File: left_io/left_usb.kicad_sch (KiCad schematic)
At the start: 160 parts, among them J22 USB-C source-only data port J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, J23 USB-C source-only data port J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, J24 USB 3.0 Type-A internal heade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, J25 USB 2.0 Type-A internal heade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, U1700 USB7206C-I/KDX six-port USB 3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, U1701 TPS62823DLC 3A USB7206C 1.146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, U1702 TLV803EA29 USB hub reset supe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, U1703 TPS56637RPAR VSYS to USB_PORT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, U1704 SN74LVC1G08 hub 3V3/core-PG r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, U1740 TPS2553DDBVR 1.3A USB branch, U1741 TPS25810RVCR Type-C DFP contr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, U1742 HD3SS6126RUAR USB3 orientatio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, U1743 TPD1S514-1YZR 5.9V VBUS OVP, U1745 TPD4E05U06 USB2/CC ESD, U1780 TPS2553DDBVR 1.3A USB branch, U1781 TPS25810RVCR Type-C DFP contr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, U1782 HD3SS6126RUAR USB3 orientatio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, U1783 TPD1S514-1YZR 5.9V VBUS OVP, U1785 TPD4E05U06 USB2/CC ESD, U1800 TPS2553DDBVR USB3-A VBUS bran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, U1801 USBLC6-2P6 USB3-A D+/D- ESD, U1802 TPD4E05U06 USB3-A SuperSpeed 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, U1803 TPS2553DDBVR USB2-A VBUS bran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, U1804 USBLC6-2P6 USB2-A D+/D- ESD, Y1700 25.000MHz 3.3V USB hub oscill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

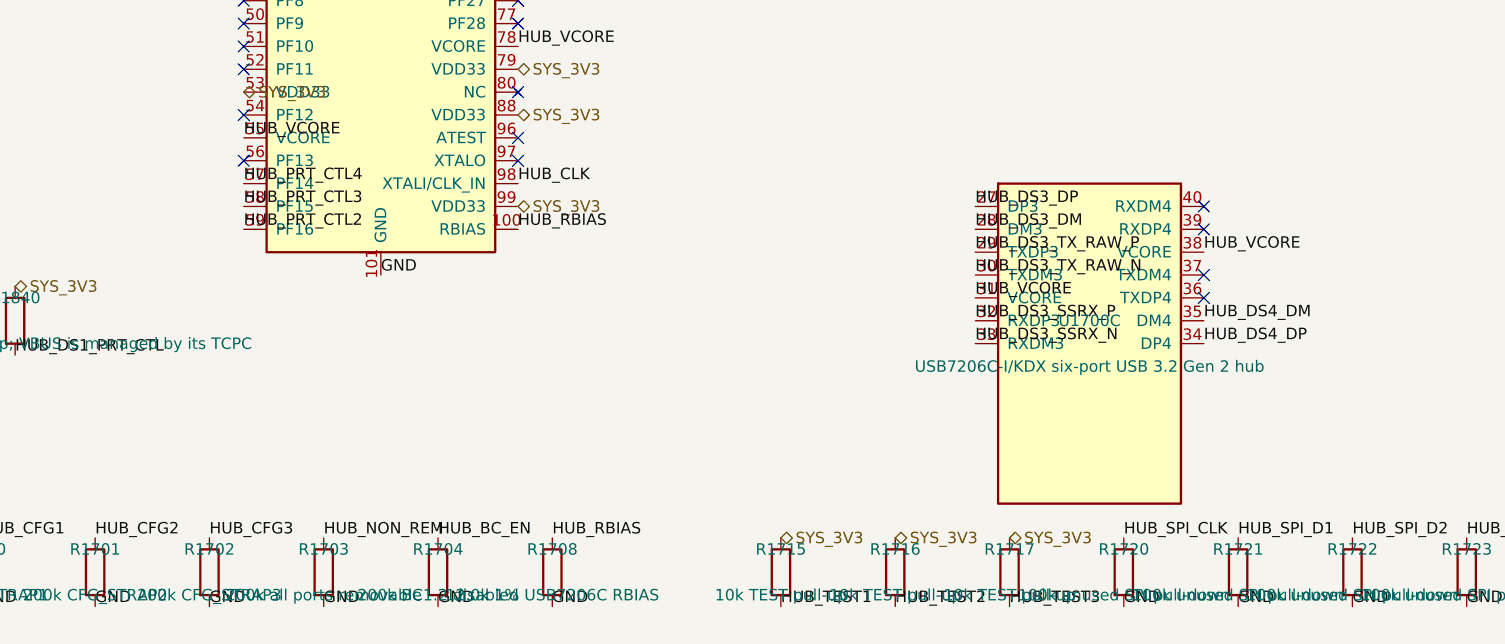
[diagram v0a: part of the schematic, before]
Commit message: Phase 5: second-opinion audit remediation + rebuilt, verified board pipeline
Second-opinion AI audit found A-tier defects; remediation applied and the
board pipeline rebuilt on a known-good base with the fixes it needed:

- electrical: LTC4418IUF symbol pinout corrected (both selectors were
  dead as drawn); center charge cascade (U15 <- U15B, PD1 > PD2 > AUX);
  pack negative never crosses FPC-3, 15-pin FG_VSS return; power-budgeted
  FPC pin maps (0.4 A/pin derate); J12/DS4 completed; AUX source fuse
- FH41-68S footprint: 13 datasheet-correct SH pads + SH pin in symbol
- connector geometry settled against the Hirose FH12 2D drawing: FFC
  enters opposite the solder pins (mouth = local +Y); reversed side-B
  maps are correct for the 180-deg-mounted pairs; rotations set so mouths
  face across every seam
- pipeline (generate_split_boards.py): per-pin pad-net resync from the
  netlists (kills shadow nets for good), netlist-exact name
  normalization, netlist-only part injection (cascade, probe headers),
  zone refill after outline swap, read-before-write race fixed, orphan
  parts dropped loudly, non-zero exit on unresolved overlaps
- monolith board relocated to old/monolith_ducktop2.kicad_pcb (placement
  oracle for the center cut only)

verified end state: 4 boards 0 shorts / 0 clearance / 0 drill, 0 boundary
crossings, 6/6 connectors contract-exact with mouths facing, 0 shadow
nets, gates PASS x4, ERC 0 x4. routing next (499 nets/board).
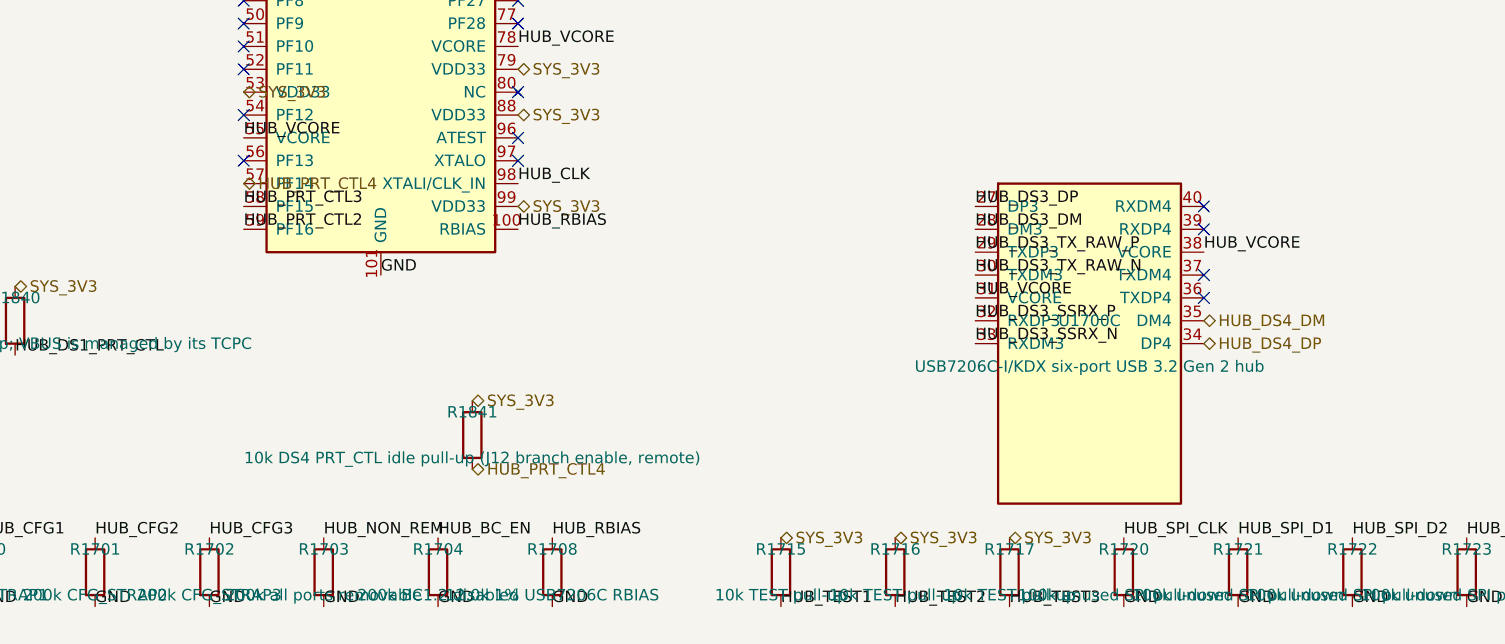
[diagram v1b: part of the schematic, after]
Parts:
- removed C1716: 100n oscillator bypass, Capacitor_SMD:C_0603_1608Metric, symbol Device:C
- removed C1717: 100n hub reset-gate bypass, Capacitor_SMD:C_0603_1608Metric, symbol Device:C
- removed C1740, C1780: 100n branch input, Capacitor_SMD:C_0603_1608Metric, symbol Device:C
- removed C1852: 100n C0G USB3-A SSTX+ series AC, Capacitor_SMD:C_0402_1005Metric, symbol Device:C
- removed R1700: 10k CFG_STRAP1, Resistor_SMD:R_0603_1608Metric, symbol Device:R
- removed R1718: 10k hub 3V3 supervisor pull-up, Resistor_SMD:R_0603_1608Metric, symbol Device:R
- removed R1740, R1780, R1850, R1851: 20.0k 1% TPS2553 1.3A ILIM, Resistor_SMD:R_0603_1608Metric, symbol Device:R
- added C1849: 10u USB7206C VDD33 bulk, Capacitor_SMD:C_0805_2012Metric, symbol Device:C
- added J24: USB 3.0 Type-A internal header (hub DIS5), Connector_USB:USB_A_Receptacle_XKB_U231-091N-4BLRA00-S, symbol USB3_A:USB3_A
- added R1723: 100k unused SPI pull-down, Resistor_SMD:R_0603_1608Metric, symbol Device:R
- added unit 2 of U1700
- added U1704: SN74LVC1G08 hub 3V3/core-PG reset gate, Package_TO_SOT_SMD:SOT-23-5, symbol 74xGxx:74LVC1G08
- added U1741, U1781: TPS25810RVCR Type-C DFP controller, Package_DFN_QFN:Texas_RVC0020A_WQFN-20-1EP_3x4mm_P0.5mm_EP1.6x2.6mm, symbol Interface_USB:TPS25810RVC
- added U1745, U1785: TPD4E05U06 USB2/CC ESD, Package_SON:USON-10_2.5x1.0mm_P0.5mm, symbol Power_Protection:TPD4E05U06DQA
- added U1801: USBLC6-2P6 USB3-A D+/D- ESD, Package_TO_SOT_SMD:SOT-666, symbol Power_Protection:USBLC6-2P6
- added U1804: USBLC6-2P6 USB2-A D+/D- ESD, Package_TO_SOT_SMD:SOT-666, symbol Power_Protection:USBLC6-2P6
- added Y1700: 25.000MHz 3.3V USB hub oscillator, Oscillator:Oscillator_SMD_Abracon_ASDMB-4Pin_2.5x2.0mm, symbol Oscillator:ASDMB-xxxMHz
- C1716: renamed from C1722; value 100n USB 3.2 TX AC coupling -> 100n oscillator bypass; footprint Capacitor_SMD:C_0402_1005Metric -> Capacitor_SMD:C_0603_1608Metric; MPN GRM155R71C104KA88D -> GRM188R71H104KA93D
- C1717: renamed from Y1700; value 25.000MHz 3.3V USB hub oscillator -> 100n hub reset-gate bypass; footprint Oscillator:Oscillator_SMD_Abracon_ASDMB-4Pin_2.5x2.0mm -> Capacitor_SMD:C_0603_1608Metric; symbol Oscillator:ASDMB-xxxMHz -> Device:C; MPN ASDMB-25.000MHZ-LC-T -> GRM188R71H104KA93D; Manufacturer Abracon -> Murata
- C1729: renamed from C1810; value 100n USB7206C VDD33 local -> 100n USB 3.2 TX AC coupling; footprint Capacitor_SMD:C_0603_1608Metric -> Capacitor_SMD:C_0402_1005Metric; MPN GRM188R71H104KA93D -> GRM155R71C104KA88D
- C1740: renamed from C1741; value 100n TPS25810 IN HF -> 100n branch input
- C1741: renamed from C1742; value 150u 10V TPS25810 input reservoir -> 100n TPS25810 IN HF; footprint Capacitor_Tantalum_SMD:CP_EIA-7343-31_Kemet-D -> Capacitor_SMD:C_0603_1608Metric; symbol Device:C_Polarized -> Device:C; MPN T520D157M010ATE025 -> GRM188R71H104KA93D; Manufacturer KEMET -> Murata
- C1742: renamed from C1743; value 10u protected VBUS_SYS -> 150u 10V TPS25810 input reservoir; footprint Capacitor_SMD:C_1206_3216Metric -> Capacitor_Tantalum_SMD:CP_EIA-7343-31_Kemet-D; symbol Device:C -> Device:C_Polarized; MPN GRM31CR71A106KA01L -> T520D157M010ATE025; Manufacturer Murata -> KEMET
- C1743: renamed from C1744; value 100n TPS25810 AUX -> 10u protected VBUS_SYS; footprint Capacitor_SMD:C_0603_1608Metric -> Capacitor_SMD:C_1206_3216Metric; MPN GRM188R71H104KA93D -> GRM31CR71A106KA01L
- C1744: renamed from C1745; value 100n mux VDD -> 100n TPS25810 AUX
- C1747: renamed from C1748; value 1u mux local bulk -> 100n mux VDD; MPN GRM188R71A105KA61D -> GRM188R71H104KA93D
- C1748: renamed from C1749; value 10n mux HF -> 1u mux local bulk; footprint Capacitor_SMD:C_0402_1005Metric -> Capacitor_SMD:C_0603_1608Metric; MPN GRM155R71H103KA88D -> GRM188R71A105KA61D
- C1749: renamed from R1741; value 4.99k POL pull-up -> 10n mux HF; footprint Resistor_SMD:R_0603_1608Metric -> Capacitor_SMD:C_0402_1005Metric; symbol Device:R -> Device:C; MPN RC0603FR-074K99L -> GRM155R71H103KA88D; Manufacturer Yageo -> Murata
- C1750: renamed from C1751; value 1u TPD1S514 VBUS_POWER stability -> 1u 50V connector-side VBUS; footprint Capacitor_SMD:C_0603_1608Metric -> Capacitor_SMD:C_0805_2012Metric; MPN GRM188R71A105KA61D -> GRM21BR71H105KA12L
- C1751: renamed from D1808; value TPD1E0B04DPLR 0.13pF USB3 ESD -> 1u TPD1S514 VBUS_POWER stability; footprint Diode_SMD:D_0201_0603Metric -> Capacitor_SMD:C_0603_1608Metric; symbol TPD1E0B04:TPD1E0B04 -> Device:C; MPN TPD1E0B04DPLR -> GRM188R71A105KA61D; Manufacturer Texas Instruments -> Murata
- C1780: renamed from C1781; value 100n TPS25810 IN HF -> 100n branch input
- C1781: renamed from C1782; value 150u 10V TPS25810 input reservoir -> 100n TPS25810 IN HF; footprint Capacitor_Tantalum_SMD:CP_EIA-7343-31_Kemet-D -> Capacitor_SMD:C_0603_1608Metric; symbol Device:C_Polarized -> Device:C; MPN T520D157M010ATE025 -> GRM188R71H104KA93D; Manufacturer KEMET -> Murata
- C1782: renamed from C1783; value 10u protected VBUS_SYS -> 150u 10V TPS25810 input reservoir; footprint Capacitor_SMD:C_1206_3216Metric -> Capacitor_Tantalum_SMD:CP_EIA-7343-31_Kemet-D; symbol Device:C -> Device:C_Polarized; MPN GRM31CR71A106KA01L -> T520D157M010ATE025; Manufacturer Murata -> KEMET
- C1783: renamed from C1784; value 100n TPS25810 AUX -> 10u protected VBUS_SYS; footprint Capacitor_SMD:C_0603_1608Metric -> Capacitor_SMD:C_1206_3216Metric; MPN GRM188R71H104KA93D -> GRM31CR71A106KA01L
- C1784: renamed from C1785; value 100n mux VDD -> 100n TPS25810 AUX
- C1787: renamed from C1788; value 1u mux local bulk -> 100n mux VDD; MPN GRM188R71A105KA61D -> GRM188R71H104KA93D
- C1788: renamed from C1789; value 10n mux HF -> 1u mux local bulk; footprint Capacitor_SMD:C_0402_1005Metric -> Capacitor_SMD:C_0603_1608Metric; MPN GRM155R71H103KA88D -> GRM188R71A105KA61D
- C1789: renamed from R1781; value 4.99k POL pull-up -> 10n mux HF; footprint Resistor_SMD:R_0603_1608Metric -> Capacitor_SMD:C_0402_1005Metric; symbol Device:R -> Device:C; MPN RC0603FR-074K99L -> GRM155R71H103KA88D; Manufacturer Yageo -> Murata
- C1790: renamed from C1791; value 1u TPD1S514 VBUS_POWER stability -> 1u 50V connector-side VBUS; footprint Capacitor_SMD:C_0603_1608Metric -> Capacitor_SMD:C_0805_2012Metric; MPN GRM188R71A105KA61D -> GRM21BR71H105KA12L
- C1791: renamed from D1800; value TPD1E0B04DPLR 0.13pF USB3 ESD -> 1u TPD1S514 VBUS_POWER stability; footprint Diode_SMD:D_0201_0603Metric -> Capacitor_SMD:C_0603_1608Metric; symbol TPD1E0B04:TPD1E0B04 -> Device:C; MPN TPD1E0B04DPLR -> GRM188R71A105KA61D; Manufacturer Texas Instruments -> Murata
- C1810: renamed from C1830; value 1n USB7206C VDD33 HF -> 100n USB7206C VDD33 local; footprint Capacitor_SMD:C_0402_1005Metric -> Capacitor_SMD:C_0603_1608Metric; MPN GRM155R71H102KA01D -> GRM188R71H104KA93D
- C1811: renamed from C1831; value 1n USB7206C VDD33 HF -> 100n USB7206C VDD33 local; footprint Capacitor_SMD:C_0402_1005Metric -> Capacitor_SMD:C_0603_1608Metric; MPN GRM155R71H102KA01D -> GRM188R71H104KA93D
- C1812: renamed from C1832; value 1n USB7206C VDD33 HF -> 100n USB7206C VDD33 local; footprint Capacitor_SMD:C_0402_1005Metric -> Capacitor_SMD:C_0603_1608Metric; MPN GRM155R71H102KA01D -> GRM188R71H104KA93D
- C1813: renamed from C1833; value 1n USB7206C VDD33 HF -> 100n USB7206C VDD33 local; footprint Capacitor_SMD:C_0402_1005Metric -> Capacitor_SMD:C_0603_1608Metric; MPN GRM155R71H102KA01D -> GRM188R71H104KA93D
- C1814: renamed from C1834; value 1n USB7206C VDD33 HF -> 100n USB7206C VDD33 local; footprint Capacitor_SMD:C_0402_1005Metric -> Capacitor_SMD:C_0603_1608Metric; MPN GRM155R71H102KA01D -> GRM188R71H104KA93D
- C1815: renamed from C1835; value 1n USB7206C VDD33 HF -> 100n USB7206C VDD33 local; footprint Capacitor_SMD:C_0402_1005Metric -> Capacitor_SMD:C_0603_1608Metric; MPN GRM155R71H102KA01D -> GRM188R71H104KA93D
- C1816: renamed from C1836; value 1n USB7206C VDD33 HF -> 100n USB7206C VDD33 local; footprint Capacitor_SMD:C_0402_1005Metric -> Capacitor_SMD:C_0603_1608Metric; MPN GRM155R71H102KA01D -> GRM188R71H104KA93D
- C1817: renamed from C1837; value 1n USB7206C VDD33 HF -> 100n USB7206C VDD33 local; footprint Capacitor_SMD:C_0402_1005Metric -> Capacitor_SMD:C_0603_1608Metric; MPN GRM155R71H102KA01D -> GRM188R71H104KA93D
- C1820: renamed from C1840; value 1n USB7206C VCORE HF -> 100n USB7206C VCORE local; footprint Capacitor_SMD:C_0402_1005Metric -> Capacitor_SMD:C_0603_1608Metric; MPN GRM155R71H102KA01D -> GRM188R71H104KA93D
- C1821: renamed from C1841; value 1n USB7206C VCORE HF -> 100n USB7206C VCORE local; footprint Capacitor_SMD:C_0402_1005Metric -> Capacitor_SMD:C_0603_1608Metric; MPN GRM155R71H102KA01D -> GRM188R71H104KA93D
- C1822: renamed from C1842; value 1n USB7206C VCORE HF -> 100n USB7206C VCORE local; footprint Capacitor_SMD:C_0402_1005Metric -> Capacitor_SMD:C_0603_1608Metric; MPN GRM155R71H102KA01D -> GRM188R71H104KA93D
- C1823: renamed from C1843; value 1n USB7206C VCORE HF -> 100n USB7206C VCORE local; footprint Capacitor_SMD:C_0402_1005Metric -> Capacitor_SMD:C_0603_1608Metric; MPN GRM155R71H102KA01D -> GRM188R71H104KA93D
- C1824: renamed from C1844; value 1n USB7206C VCORE HF -> 100n USB7206C VCORE local; footprint Capacitor_SMD:C_0402_1005Metric -> Capacitor_SMD:C_0603_1608Metric; MPN GRM155R71H102KA01D -> GRM188R71H104KA93D
- C1825: renamed from C1845; value 1n USB7206C VCORE HF -> 100n USB7206C VCORE local; footprint Capacitor_SMD:C_0402_1005Metric -> Capacitor_SMD:C_0603_1608Metric; MPN GRM155R71H102KA01D -> GRM188R71H104KA93D
- C1826: renamed from C1846; value 1n USB7206C VCORE HF -> 100n USB7206C VCORE local; footprint Capacitor_SMD:C_0402_1005Metric -> Capacitor_SMD:C_0603_1608Metric; MPN GRM155R71H102KA01D -> GRM188R71H104KA93D
- C1827: renamed from C1847; value 1n USB7206C VCORE HF -> 100n USB7206C VCORE local; footprint Capacitor_SMD:C_0402_1005Metric -> Capacitor_SMD:C_0603_1608Metric; MPN GRM155R71H102KA01D -> GRM188R71H104KA93D
- C1828: renamed from C1848; value 1n USB7206C VCORE HF -> 100n USB7206C VCORE local; footprint Capacitor_SMD:C_0402_1005Metric -> Capacitor_SMD:C_0603_1608Metric; MPN GRM155R71H102KA01D -> GRM188R71H104KA93D
- C1830: renamed from C1811; value 100n USB7206C VDD33 local -> 1n USB7206C VDD33 HF; footprint Capacitor_SMD:C_0603_1608Metric -> Capacitor_SMD:C_0402_1005Metric; MPN GRM188R71H104KA93D -> GRM155R71H102KA01D
- C1831: renamed from C1812; value 100n USB7206C VDD33 local -> 1n USB7206C VDD33 HF; footprint Capacitor_SMD:C_0603_1608Metric -> Capacitor_SMD:C_0402_1005Metric; MPN GRM188R71H104KA93D -> GRM155R71H102KA01D
- C1832: renamed from C1813; value 100n USB7206C VDD33 local -> 1n USB7206C VDD33 HF; footprint Capacitor_SMD:C_0603_1608Metric -> Capacitor_SMD:C_0402_1005Metric; MPN GRM188R71H104KA93D -> GRM155R71H102KA01D
- C1833: renamed from C1814; value 100n USB7206C VDD33 local -> 1n USB7206C VDD33 HF; footprint Capacitor_SMD:C_0603_1608Metric -> Capacitor_SMD:C_0402_1005Metric; MPN GRM188R71H104KA93D -> GRM155R71H102KA01D
- C1834: renamed from C1815; value 100n USB7206C VDD33 local -> 1n USB7206C VDD33 HF; footprint Capacitor_SMD:C_0603_1608Metric -> Capacitor_SMD:C_0402_1005Metric; MPN GRM188R71H104KA93D -> GRM155R71H102KA01D
- C1835: renamed from C1816; value 100n USB7206C VDD33 local -> 1n USB7206C VDD33 HF; footprint Capacitor_SMD:C_0603_1608Metric -> Capacitor_SMD:C_0402_1005Metric; MPN GRM188R71H104KA93D -> GRM155R71H102KA01D
- C1836: renamed from C1817; value 100n USB7206C VDD33 local -> 1n USB7206C VDD33 HF; footprint Capacitor_SMD:C_0603_1608Metric -> Capacitor_SMD:C_0402_1005Metric; MPN GRM188R71H104KA93D -> GRM155R71H102KA01D
- C1837: renamed from C1820; value 100n USB7206C VCORE local -> 1n USB7206C VDD33 HF; footprint Capacitor_SMD:C_0603_1608Metric -> Capacitor_SMD:C_0402_1005Metric; MPN GRM188R71H104KA93D -> GRM155R71H102KA01D
- C1840: renamed from C1821; value 100n USB7206C VCORE local -> 1n USB7206C VCORE HF; footprint Capacitor_SMD:C_0603_1608Metric -> Capacitor_SMD:C_0402_1005Metric; MPN GRM188R71H104KA93D -> GRM155R71H102KA01D
- C1841: renamed from C1822; value 100n USB7206C VCORE local -> 1n USB7206C VCORE HF; footprint Capacitor_SMD:C_0603_1608Metric -> Capacitor_SMD:C_0402_1005Metric; MPN GRM188R71H104KA93D -> GRM155R71H102KA01D
- C1842: renamed from C1823; value 100n USB7206C VCORE local -> 1n USB7206C VCORE HF; footprint Capacitor_SMD:C_0603_1608Metric -> Capacitor_SMD:C_0402_1005Metric; MPN GRM188R71H104KA93D -> GRM155R71H102KA01D
- C1843: renamed from C1824; value 100n USB7206C VCORE local -> 1n USB7206C VCORE HF; footprint Capacitor_SMD:C_0603_1608Metric -> Capacitor_SMD:C_0402_1005Metric; MPN GRM188R71H104KA93D -> GRM155R71H102KA01D
- C1844: renamed from C1825; value 100n USB7206C VCORE local -> 1n USB7206C VCORE HF; footprint Capacitor_SMD:C_0603_1608Metric -> Capacitor_SMD:C_0402_1005Metric; MPN GRM188R71H104KA93D -> GRM155R71H102KA01D
- C1845: renamed from C1826; value 100n USB7206C VCORE local -> 1n USB7206C VCORE HF; footprint Capacitor_SMD:C_0603_1608Metric -> Capacitor_SMD:C_0402_1005Metric; MPN GRM188R71H104KA93D -> GRM155R71H102KA01D
- C1846: renamed from C1827; value 100n USB7206C VCORE local -> 1n USB7206C VCORE HF; footprint Capacitor_SMD:C_0603_1608Metric -> Capacitor_SMD:C_0402_1005Metric; MPN GRM188R71H104KA93D -> GRM155R71H102KA01D
- C1847: renamed from C1828; value 100n USB7206C VCORE local -> 1n USB7206C VCORE HF; footprint Capacitor_SMD:C_0603_1608Metric -> Capacitor_SMD:C_0402_1005Metric; MPN GRM188R71H104KA93D -> GRM155R71H102KA01D
- C1848: renamed from C1849; value 10u USB7206C VDD33 bulk -> 1n USB7206C VCORE HF; footprint Capacitor_SMD:C_0805_2012Metric -> Capacitor_SMD:C_0402_1005Metric; MPN GRM21BR71A106KE51L -> GRM155R71H102KA01D
- C1850: renamed from C1851; value 100n USB3-A VBUS HF -> 10u 10V USB3-A VBUS bulk; footprint Capacitor_SMD:C_0603_1608Metric -> Capacitor_SMD:C_1206_3216Metric; MPN GRM188R71H104KA93D -> GRM21BR71A106KA73L
- C1851: renamed from U1801; value USBLC6-2P6 USB3-A D+/D- ESD -> 100n USB3-A VBUS HF; footprint Package_TO_SOT_SMD:SOT-666 -> Capacitor_SMD:C_0603_1608Metric; symbol Power_Protection:USBLC6-2P6 -> Device:C; MPN USBLC6-2P6 -> GRM188R71H104KA93D; Manufacturer STMicroelectronics -> Murata
- C1852: renamed from C1853; value 100n C0G USB3-A SSTX- series AC -> 100n C0G USB3-A SSTX+ series AC
- C1853: renamed from J24; value USB 3.0 Type-A internal header (hub DIS5) -> 100n C0G USB3-A SSTX- series AC; footprint Connector_USB:USB_A_Receptacle_XKB_U231-091N-4BLRA00-S -> Capacitor_SMD:C_0402_1005Metric; symbol USB3_A:USB3_A -> Device:C; MPN U231-091N-4BLRA00-S -> GRM1555C1H101JA01D; Manufacturer XKB Connectivity -> Murata
- C1854: renamed from C1855; value 100n USB2-A VBUS HF -> 10u 10V USB2-A VBUS bulk; footprint Capacitor_SMD:C_0603_1608Metric -> Capacitor_SMD:C_1206_3216Metric; MPN GRM188R71H104KA93D -> GRM21BR71A106KA73L
- C1855: renamed from U1804; value USBLC6-2P6 USB2-A D+/D- ESD -> 100n USB2-A VBUS HF; footprint Package_TO_SOT_SMD:SOT-666 -> Capacitor_SMD:C_0603_1608Metric; symbol Power_Protection:USBLC6-2P6 -> Device:C; MPN USBLC6-2P6 -> GRM188R71H104KA93D; Manufacturer STMicroelectronics -> Murata
- D1807: renamed from U1785; value TPD4E05U06 USB2/CC ESD -> TPD1E0B04DPLR 0.13pF USB3 ESD; footprint Package_SON:USON-10_2.5x1.0mm_P0.5mm -> Diode_SMD:D_0201_0603Metric; symbol Power_Protection:TPD4E05U06DQA -> TPD1E0B04:TPD1E0B04; MPN TPD4E05U06DQAR -> TPD1E0B04DPLR
- D1815: renamed from U1745; value TPD4E05U06 USB2/CC ESD -> TPD1E0B04DPLR 0.13pF USB3 ESD; footprint Package_SON:USON-10_2.5x1.0mm_P0.5mm -> Diode_SMD:D_0201_0603Metric; symbol Power_Protection:TPD4E05U06DQA -> TPD1E0B04:TPD1E0B04; MPN TPD4E05U06DQAR -> TPD1E0B04DPLR
- R1700: renamed from R1701; value 200k CFG_STRAP2 -> 10k CFG_STRAP1; MPN RC0603FR-07200KL -> RC0603FR-0710KL
- R1701: renamed from R1702; value 200k CFG_STRAP3 -> 200k CFG_STRAP2
- R1702: renamed from R1703; value 200k all ports removable -> 200k CFG_STRAP3
- R1703: renamed from R1704; value 200k BC1.2 disabled -> 200k all ports removable
- R1704: renamed from R1708; value 12.0k 1% USB7206C RBIAS -> 200k BC1.2 disabled; MPN RC0603FR-0712KL -> RC0603FR-07200KL
- R1708: renamed from R1715; value 10k TEST pull-up -> 12.0k 1% USB7206C RBIAS; MPN RC0603FR-0710KL -> RC0603FR-0712KL
- R1717: renamed from R1720; value 100k unused SPI pull-down -> 10k TEST pull-up; MPN RC0603FR-07100KL -> RC0603FR-0710KL
- R1718: renamed from U1704; value SN74LVC1G08 hub 3V3/core-PG reset gate -> 10k hub 3V3 supervisor pull-up; footprint Package_TO_SOT_SMD:SOT-23-5 -> Resistor_SMD:R_0603_1608Metric; symbol 74xGxx:74LVC1G08 -> Device:R; MPN SN74LVC1G08DBVR -> RC0603FR-0710KL; Manufacturer Texas Instruments -> Yageo
- R1740: renamed from U1741; value TPS25810RVCR Type-C DFP controller -> 20.0k 1% TPS2553 1.3A ILIM; footprint Package_DFN_QFN:Texas_RVC0020A_WQFN-20-1EP_3x4mm_P0.5mm_EP1.6x2.6mm -> Resistor_SMD:R_0603_1608Metric; symbol Interface_USB:TPS25810RVC -> Device:R; MPN TPS25810RVCR -> RC0603FR-0720KL; Manufacturer Texas Instruments -> Yageo
- R1741: renamed from R1742; value 100k 1% TPS25810 REF -> 4.99k POL pull-up; MPN RC0603FR-07100KL -> RC0603FR-074K99L
- R1742: renamed from R1750; value 249R 0.25W TPS25810 OUT discharge -> 100k 1% TPS25810 REF; footprint Resistor_SMD:R_1206_3216Metric -> Resistor_SMD:R_0603_1608Metric; MPN RC1206FR-07249RL -> RC0603FR-07100KL
- R1750: renamed from C1750; value 1u 50V connector-side VBUS -> 249R 0.25W TPS25810 OUT discharge; footprint Capacitor_SMD:C_0805_2012Metric -> Resistor_SMD:R_1206_3216Metric; symbol Device:C -> Device:R; MPN GRM21BR71H105KA12L -> RC1206FR-07249RL; Manufacturer Murata -> Yageo
- R1780: renamed from U1781; value TPS25810RVCR Type-C DFP controller -> 20.0k 1% TPS2553 1.3A ILIM; footprint Package_DFN_QFN:Texas_RVC0020A_WQFN-20-1EP_3x4mm_P0.5mm_EP1.6x2.6mm -> Resistor_SMD:R_0603_1608Metric; symbol Interface_USB:TPS25810RVC -> Device:R; MPN TPS25810RVCR -> RC0603FR-0720KL; Manufacturer Texas Instruments -> Yageo
- R1781: renamed from R1782; value 100k 1% TPS25810 REF -> 4.99k POL pull-up; MPN RC0603FR-07100KL -> RC0603FR-074K99L
- R1782: renamed from R1790; value 249R 0.25W TPS25810 OUT discharge -> 100k 1% TPS25810 REF; footprint Resistor_SMD:R_1206_3216Metric -> Resistor_SMD:R_0603_1608Metric; MPN RC1206FR-07249RL -> RC0603FR-07100KL
- R1790: renamed from C1790; value 1u 50V connector-side VBUS -> 249R 0.25W TPS25810 OUT discharge; footprint Capacitor_SMD:C_0805_2012Metric -> Resistor_SMD:R_1206_3216Metric; symbol Device:C -> Device:R; MPN GRM21BR71H105KA12L -> RC1206FR-07249RL; Manufacturer Murata -> Yageo
- R1841: renamed from U1700; value USB7206C-I/KDX six-port USB 3.2 Gen 2 hub -> 10k DS4 PRT_CTL idle pull-up (J12 branch enable, remote); footprint Package_DFN_QFN:VQFN-100-1EP_12x12mm_P0.4mm_EP8x8mm_ThermalVias -> Resistor_SMD:R_0603_1608Metric; symbol USB7206C:USB7206C -> Device:R; MPN USB7206C-I/KDX -> RC0603FR-0710KL; Manufacturer Microchip -> Yageo
- R1850: renamed from C1850; value 10u 10V USB3-A VBUS bulk -> 20.0k 1% TPS2553 1.3A ILIM; footprint Capacitor_SMD:C_1206_3216Metric -> Resistor_SMD:R_0603_1608Metric; symbol Device:C -> Device:R; MPN GRM21BR71A106KA73L -> RC0603FR-0720KL; Manufacturer Murata -> Yageo
- R1851: renamed from C1854; value 10u 10V USB2-A VBUS bulk -> 20.0k 1% TPS2553 1.3A ILIM; footprint Capacitor_SMD:C_1206_3216Metric -> Resistor_SMD:R_0603_1608Metric; symbol Device:C -> Device:R; MPN GRM21BR71A106KA73L -> RC0603FR-0720KL; Manufacturer Murata -> Yageo
- renumbered C1723 to C1722, C1724 to C1723, C1725 to C1724, C1728 to C1725, C1729 to C1728, C1746 to C1745, C1747 to C1746, C1786 to C1785, C1787 to C1786, D1801 to D1800, D1802 to D1801, D1803 to D1802, D1804 to D1803, D1805 to D1804, D1806 to D1805, D1807 to D1806, D1809 to D1808, D1810 to D1809, D1811 to D1810, D1812 to D1811, D1813 to D1812, D1814 to D1813, D1815 to D1814, R1716 to R1715, R1717 to R1716, R1721 to R1720, R1722 to R1721, R1723 to R1722
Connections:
- net GND: now also C1716.2, C1749.2, C1789.2, D1807.2 (IO), D1815.2 (IO), R1708.2, R1740.2, R1780.2, C1849.2, J24.4 (GND), J24.7 (GND_DRAIN), J24.SH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; no longer C1729.2, C1851.5 (VBUS), C1853.4 (GND), C1853.7 (GND_DRAIN), C1853.SH, C1855.5 (VBUS), D1807.3 (GND), D1807.8 (GND), D1815.3 (GND), D1815.8 (GND), R1717.2, R1718.3 (GND)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
- net HUB_3V3_OK: now also R1718.2, U1704.1; no longer R1718.1
- net HUB_BC_EN: now also R1704.1; no longer R1703.1
- net HUB_CFG1: now also R1700.1
- net HUB_CFG2: now also R1701.1; no longer R1700.1
- net HUB_CFG3: now also R1702.1; no longer R1701.1
- net HUB_CLK: now also Y1700.3 (Out); no longer C1717.3 (Out)
- net HUB_CORE_PG: now also U1704.2; no longer R1718.2
- net HUB_DIS5_DM: now also J24.2 (D-), U1801.3 (I/O2), U1801.4 (I/O2); no longer C1851.3 (I/O2), C1851.4 (I/O2), C1853.2 (D-)
- net HUB_DIS5_DP: now also J24.3 (D+), U1801.1 (I/O1), U1801.6 (I/O1); no longer C1851.1 (I/O1), C1851.6 (I/O1), C1853.3 (D+)
- net HUB_DIS5_RX_N: now also J24.5 (StdA_SSRX-); no longer C1853.5 (StdA_SSRX-)
- net HUB_DIS5_RX_P: now also J24.6 (StdA_SSRX+); no longer C1853.6 (StdA_SSRX+)
- net HUB_DIS5_TX_N: now also C1853.1; no longer C1852.1
- net HUB_DIS5_TX_P: now also C1852.1
- net HUB_DIS6_DM: now also U1804.3 (I/O2), U1804.4 (I/O2); no longer C1855.3 (I/O2), C1855.4 (I/O2)
- net HUB_DIS6_DP: now also U1804.1 (I/O1), U1804.6 (I/O1); no longer C1855.1 (I/O1), C1855.6 (I/O1)
- net HUB_DS1_DM: now also U1700.6 (DM1); no longer R1841.6 (DM1)
- net HUB_DS1_DP: now also U1700.5 (DP1); no longer R1841.5 (DP1)
- net HUB_DS2_DM: now also U1700.15 (DM2), U1785.2 (D1-); no longer D1807.2 (D1-), R1841.15 (DM2)
- net HUB_DS2_DP: now also U1700.14 (DP2), U1785.1 (D1+); no longer D1807.1 (D1+), R1841.14 (DP2)
- net HUB_DS2_SSRX_N: now also U1700.20 (RXDM2); no longer R1841.20 (RXDM2)
- net HUB_DS2_SSRX_P: now also U1700.19 (RXDP2); no longer R1841.19 (RXDP2)
- net HUB_DS2_SSTX_N: now also C1723.2; no longer C1722.2
- net HUB_DS2_SSTX_P: now also C1722.2; no longer C1716.2
- net HUB_DS2_TX_RAW_N: now also C1723.1, U1700.17 (TXDM2); no longer C1722.1, R1841.17 (TXDM2)
- net HUB_DS2_TX_RAW_P: now also C1722.1, U1700.16 (TXDP2); no longer C1716.1, R1841.16 (TXDP2)
- net HUB_DS3_DM: now also U1745.2 (D1-); no longer D1815.2 (D1-)
- net HUB_DS3_DP: now also U1745.1 (D1+); no longer D1815.1 (D1+)
- net HUB_DS3_SSTX_N: now also C1725.2; no longer C1724.2
- net HUB_DS3_SSTX_P: now also C1724.2; no longer C1723.2
- net HUB_DS3_TX_RAW_N: now also C1725.1; no longer C1724.1
- net HUB_DS3_TX_RAW_P: now also C1724.1; no longer C1723.1
- net HUB_NON_REM: now also R1703.1; no longer R1702.1
- net HUB_PRT_CTL2: now also U1781.1 (~{FAULT}), U1781.6 (EN); no longer R1780.1 (~{FAULT}), R1780.6 (EN)
- net HUB_PRT_CTL3: now also U1741.1 (~{FAULT}), U1741.6 (EN); no longer R1740.1 (~{FAULT}), R1740.6 (EN)
- net HUB_PRT_CTL4: now also R1841.2
- net HUB_RBIAS: now also R1708.1; no longer R1704.1
- net HUB_RESET_N: now also U1704.4; no longer R1718.4
- net HUB_SPI_CLK: now also R1720.1; no longer R1717.1
- net HUB_SPI_D1: now also R1721.1; no longer R1720.1
- net HUB_SPI_D2: now also R1722.1; no longer R1721.1
- net HUB_SPI_D3: now also R1723.1; no longer R1722.1
- net HUB_TEST1: now also R1715.2; no longer R1708.2
- net HUB_TEST2: now also R1716.2; no longer R1715.2
- net HUB_TEST3: now also R1717.2; no longer R1716.2
- net HUB_UP_TX_RAW_N: now also C1729.1; no longer C1728.1
- net HUB_UP_TX_RAW_P: now also C1728.1; no longer C1725.1
- net HUB_VCORE: now also C1848.1, U1700.18 (VCORE), U1700.9 (VCORE); no longer C1837.1, R1841.18 (VCORE), R1841.9 (VCORE)
- net J22_5V_PRE: now also C1782.1, U1781.2 (IN1), U1781.3 (IN1), U1781.4 (IN2); no longer C1780.1, R1780.2 (IN1), R1780.3 (IN1), R1780.4 (IN2)
- net J22_CC1: now also U1781.11 (CC1), U1785.4 (D2+); no longer D1807.4 (D2+), R1780.11 (CC1)
- net J22_CC2: now also U1781.13 (CC2), U1785.5 (D2-); no longer D1807.5 (D2-), R1780.13 (CC2)
- net J22_ILIM: now also R1780.1
- net J22_POL_N: now also R1781.2, U1781.18 (~{POL}); no longer C1789.2, R1780.18 (~{POL})
- net J22_REF: now also R1782.1, U1781.10 (REF); no longer R1780.10 (REF), R1781.1
- net J22_REF_RTN: now also R1782.2, U1781.9 (REF_RTN); no longer R1780.9 (REF_RTN), R1781.2
- net J22_RX1_N: now also D1805.1 (IO); no longer D1804.1 (IO)
- net J22_RX1_P: now also D1804.1 (IO); no longer D1803.1 (IO)
- net J22_RX2_N: now also D1807.1 (IO); no longer D1806.1 (IO)
- net J22_RX2_P: now also D1806.1 (IO); no longer D1805.1 (IO)
- net J22_TX1_N: now also D1801.1 (IO); no longer D1800.1 (IO)
- net J22_TX1_P: now also D1800.1 (IO); no longer C1791.1 (IO)
- net J22_TX2_N: now also D1803.1 (IO); no longer D1802.1 (IO)
- net J22_TX2_P: now also D1802.1 (IO); no longer D1801.1 (IO)
- net J22_VBUS: now also C1790.1; no longer R1790.1
- net J22_VBUS_POWER: now also C1791.1; no longer C1790.1
- net J22_VBUS_SYS: now also C1783.1, R1790.1, U1781.14 (OUT), U1781.15 (OUT); no longer C1782.1, R1780.14 (OUT), R1780.15 (OUT), R1782.1
- net J23_5V_PRE: now also C1742.1, U1741.2 (IN1), U1741.3 (IN1), U1741.4 (IN2); no longer C1740.1, R1740.2 (IN1), R1740.3 (IN1), R1740.4 (IN2)
- net J23_CC1: now also U1741.11 (CC1), U1745.4 (D2+); no longer D1815.4 (D2+), R1740.11 (CC1)
- net J23_CC2: now also U1741.13 (CC2), U1745.5 (D2-); no longer D1815.5 (D2-), R1740.13 (CC2)
- net J23_ILIM: now also R1740.1
- net J23_POL_N: now also R1741.2, U1741.18 (~{POL}); no longer C1749.2, R1740.18 (~{POL})
- net J23_REF: now also R1742.1, U1741.10 (REF); no longer R1740.10 (REF), R1741.1
- net J23_REF_RTN: now also R1742.2, U1741.9 (REF_RTN); no longer R1740.9 (REF_RTN), R1741.2
- net J23_RX1_N: now also D1813.1 (IO); no longer D1812.1 (IO)
- net J23_RX1_P: now also D1812.1 (IO); no longer D1811.1 (IO)
- net J23_RX2_N: now also D1815.1 (IO); no longer D1814.1 (IO)
- net J23_RX2_P: now also D1814.1 (IO); no longer D1813.1 (IO)
- net J23_TX1_N: now also D1809.1 (IO); no longer D1808.1 (IO)
- net J23_TX1_P: now also D1808.1 (IO); no longer C1751.1 (IO)
- net J23_TX2_N: now also D1811.1 (IO); no longer D1810.1 (IO)
- net J23_TX2_P: now also D1810.1 (IO); no longer D1809.1 (IO)
- net J23_VBUS: now also C1750.1; no longer R1750.1
- net J23_VBUS_POWER: now also C1751.1; no longer C1750.1
- net J23_VBUS_SYS: now also C1743.1, R1750.1, U1741.14 (OUT), U1741.15 (OUT); no longer C1742.1, R1740.14 (OUT), R1740.15 (OUT), R1742.1
- net J24_5V_PRE: now also C1851.1, J24.1 (VBUS); no longer C1853.1 (VBUS), R1850.1
- net J24_ILIM: now also R1850.1
- net J24_SSTX_N: now also C1853.2, J24.8 (StdA_SSTX-); no longer C1852.2, C1853.8 (StdA_SSTX-)
- net J24_SSTX_P: now also C1852.2, J24.9 (StdA_SSTX+); no longer C1853.9 (StdA_SSTX+)
- net J25_5V_PRE: now also C1855.1; no longer R1851.1
- net J25_ILIM: now also R1851.1
- net SYS_3V3: now also C1716.1, C1837.1, R1717.1, R1718.1, R1741.1, R1781.1, R1841.1, C1849.1, U1704.5 (VCC), U1741.5 (AUX), U1781.5 (AUX), Y1700.1 (Standby)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; no longer C1717.4 (VDD), C1729.1, C1743.1, C1783.1, C1848.1, R1708.1, R1718.5 (VCC), R1740.5 (AUX), R1780.5 (AUX)
- net USBC2_SSRX_N: now also C1729.2; no longer C1728.2
- net USBC2_SSRX_P: now also C1728.2; no longer C1725.2
- net USB_PORT_5V: now also C1740.1, C1780.1
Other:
- moved on the sheet: C1716, C1722, C1723, C1724, C1725, C1728, C1729, C1740, C1743, C1744, C1745, C1746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
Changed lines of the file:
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@@
 )
 (no_connect (at 330.2 114.3))
-(label "HUB_PRT_CTL4"
+(hierarchical_label "HUB_PRT_CTL4"
+  (shape bidirectional)
   (at 330.2 116.84 0)
   (effects (font (size 1.27 1.27)) (justify left bottom))
@@
 (label "HUB_DS1_PRT_CTL"
   (at 304.8 135.89 0)
+  (effects (font (size 1.27 1.27)) (justify left bottom))
+)
+(symbol
+  (lib_id "Device:R")
+  (at 355.6 144.78 0)
+  (unit 1)
+  (exclude_from_sim no)
+  (in_bom yes)
+  (on_board yes)
+  (dnp no)
+  (property "Reference" "R1841" (at 355.6 142.24 0) (effects (font (size 1.27 1.27))))
+  (property "Value" "10k DS4 PRT_CTL idle pull-up (J12 branch enable, remote)" (at 355.6 147.32 0) (effects (font (size 1.27 1.27))))
+  (property "Footprint" "Resistor_SMD:R_0603_1608Metric" (at 355.6 144.78 0) (effects (font (size 1.27 1.27)) (hide yes)))
+  (property "Datasheet" "" (at 355.6 144.78 0) (effects (font (size 1.27 1.27)) (hide yes)))
+  (property "Manufacturer" "Yageo" (at 355.6 144.78 0) (effects (font (size 1.27 1.27)) (hide yes)))
+  (property "MPN" "RC0603FR-0710KL" (at 355.6 144.78 0) (effects (font (size 1.27 1.27)) (hide yes)))
+  (pin "1")
+  (pin "2")
+  (instances
+    (project "ducktop2"
+      (path "/f49c1072-f547-5a4f-a0ae-12bbf6096b8e"
+        (reference "R1841")
+        (unit 1)
+      )
+    )
+  )
+)
+(hierarchical_label "SYS_3V3"
+  (shape bidirectional)
+  (at 355.6 140.97 0)
+  (effects (font (size 1.27 1.27)) (justify left bottom))
+)
+(hierarchical_label "HUB_PRT_CTL4"
+  (shape bidirectional)
+  (at 355.6 148.59 0)
   (effects (font (size 1.27 1.27)) (justify left bottom))
 )
@@
   (effects (font (size 1.27 1.27)) (justify left bottom))
 )
-(label "HUB_DS4_DP"
+(hierarchical_label "HUB_DS4_DP"
+  (shape bidirectional)
   (at 436.88 134.62 0)
   (effects (font (size 1.27 1.27)) (justify left bottom))
 )
-(label "HUB_DS4_DM"
+(hierarchical_label "HUB_DS4_DM"
+  (shape bidirectional)
   (at 436.88 132.08 0)
   (effects (font (size 1.27 1.27)) (justify left bottom))

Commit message: get the main boards ready for routing
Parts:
- C1852: value 100n C0G USB3-A SSTX+ series AC -> 100n 16V X7R USB3-A SSTX+ series AC; MPN GRM1555C1H101JA01D -> GRM155R71C104KA88D
- C1853: value 100n C0G USB3-A SSTX- series AC -> 100n 16V X7R USB3-A SSTX- series AC; MPN GRM1555C1H101JA01D -> GRM155R71C104KA88D
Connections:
- net HUB_DIS5_DM renamed HUB_DIS5_DN
- net HUB_DIS6_DM renamed HUB_DIS6_DN
- net HUB_DS1_DM renamed HUB_DS1_DN
- net HUB_DS2_DM renamed HUB_DS2_DN
- net HUB_DS3_DM renamed HUB_DS3_DN
- net HUB_DS4_DM renamed HUB_DS4_DN
- net USBC2_DM renamed USBC2_DN
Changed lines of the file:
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@@
   (effects (font (size 1.27 1.27)) (justify left bottom))
 )
-(hierarchical_label "HUB_DS1_DM"
+(hierarchical_label "HUB_DS1_DN"
   (shape bidirectional)
   (at 411.48 48.26 0)
@@
   (effects (font (size 1.27 1.27)) (justify left bottom))
 )
-(label "HUB_DS2_DM"
+(label "HUB_DS2_DN"
   (at 436.88 58.42 0)
   (effects (font (size 1.27 1.27)) (justify left bottom))
@@
   (effects (font (size 1.27 1.27)) (justify left bottom))
 )
-(label "HUB_DS3_DM"
+(label "HUB_DS3_DN"
   (at 411.48 121.92 0)
   (effects (font (size 1.27 1.27)) (justify left bottom))
@@
   (effects (font (size 1.27 1.27)) (justify left bottom))
 )
-(hierarchical_label "HUB_DS4_DM"
+(hierarchical_label "HUB_DS4_DN"
   (shape bidirectional)
   (at 436.88 132.08 0)
@@
   )
 )
-(label "HUB_DIS6_DM"
+(label "HUB_DIS6_DN"
   (at 487.68 53.34 0)
   (effects (font (size 1.27 1.27)) (justify left bottom))
@@
   (effects (font (size 1.27 1.27)) (justify left bottom))
 )
-(label "HUB_DIS5_DM"
+(label "HUB_DIS5_DN"
   (at 513.08 55.88 0)
   (effects (font (size 1.27 1.27)) (justify left bottom))
@@
   (effects (font (size 1.27 1.27)) (justify left bottom))
 )
-(hierarchical_label "USBC2_DM"
+(hierarchical_label "USBC2_DN"
   (shape bidirectional)
   (at 487.68 129.54 0)
@@
   (effects (font (size 1.27 1.27)) (justify left bottom))
 )
-(label "HUB_DIS5_DM"
+(label "HUB_DIS5_DN"
   (at 154.94 335.28 0)
   (effects (font (size 1.27 1.27)) (justify left bottom))
 )
-(label "HUB_DIS5_DM"
+(label "HUB_DIS5_DN"
   (at 165.1 335.28 0)
   (effects (font (size 1.27 1.27)) (justify left bottom))
@@
   (dnp no)
   (property "Reference" "C1852" (at 250.19 341.63 0) (effects (font (size 1.27 1.27))))
-  (property "Value" "100n C0G USB3-A SSTX+ series AC" (at 250.19 346.71 0) (effects (font (size 1.27 1.27))))
+  (property "Value" "100n 16V X7R USB3-A SSTX+ series AC" (at 250.19 346.71 0) (effects (font (size 1.27 1.27))))
   (property "Footprint" "Capacitor_SMD:C_0402_1005Metric" (at 250.19 344.17 0) (effects (font (size 1.27 1.27)) (hide yes)))
   (property "Datasheet" "" (at 250.19 344.17 0) (effects (font (size 1.27 1.27)) (hide yes)))
   (property "Manufacturer" "Murata" (at 250.19 344.17 0) (effects (font (size 1.27 1.27)) (hide yes)))
-  (property "MPN" "GRM1555C1H101JA01D" (at 250.19 344.17 0) (effects (font (size 1.27 1.27)) (hide yes)))
+  (property "MPN" "GRM155R71C104KA88D" (at 250.19 344.17 0) (effects (font (size 1.27 1.27)) (hide yes)))
   (pin "1")
   (pin "2")
@@
   (dnp no)
   (property "Reference" "C1853" (at 250.19 353.06 0) (effects (font (size 1.27 1.27))))
-  (property "Value" "100n C0G USB3-A SSTX- series AC" (at 250.19 358.14 0) (effects (font (size 1.27 1.27))))
+  (property "Value" "100n 16V X7R USB3-A SSTX- series AC" (at 250.19 358.14 0) (effects (font (size 1.27 1.27))))
   (property "Footprint" "Capacitor_SMD:C_0402_1005Metric" (at 250.19 355.6 0) (effects (font (size 1.27 1.27)) (hide yes)))
   (property "Datasheet" "" (at 250.19 355.6 0) (effects (font (size 1.27 1.27)) (hide yes)))
   (property "Manufacturer" "Murata" (at 250.19 355.6 0) (effects (font (size 1.27 1.27)) (hide yes)))
-  (property "MPN" "GRM1555C1H101JA01D" (at 250.19 355.6 0) (effects (font (size 1.27 1.27)) (hide yes)))
+  (property "MPN" "GRM155R71C104KA88D" (at 250.19 355.6 0) (effects (font (size 1.27 1.27)) (hide yes)))
   (pin "1")
   (pin "2")
@@
   (effects (font (size 1.27 1.27)) (justify left bottom))
 )
-(label "HUB_DIS5_DM"
+(label "HUB_DIS5_DN"
   (at 330.2 330.2 0)
   (effects (font (size 1.27 1.27)) (justify left bottom))
@@
   (effects (font (size 1.27 1.27)) (justify left bottom))
 )
-(label "HUB_DIS6_DM"
+(label "HUB_DIS6_DN"
   (at 154.94 403.86 0)
   (effects (font (size 1.27 1.27)) (justify left bottom))
 )
-(label "HUB_DIS6_DM"
+(label "HUB_DIS6_DN"
   (at 165.1 403.86 0)
   (effects (font (size 1.27 1.27)) (justify left bottom))
@@
   (effects (font (size 1.27 1.27)) (justify left bottom))
 )
-(label "HUB_DIS6_DM"
+(label "HUB_DIS6_DN"
   (at 347.98 408.94 0)
   (effects (font (size 1.27 1.27)) (justify left bottom))
@@
   (effects (font (size 1.27 1.27)) (justify left bottom))
 )
-(label "HUB_DS2_DM"
+(label "HUB_DS2_DN"
   (at 261.62 269.24 0)
   (effects (font (size 1.27 1.27)) (justify left bottom))
 )
-(label "HUB_DS2_DM"
+(label "HUB_DS2_DN"
   (at 261.62 271.78 0)
   (effects (font (size 1.27 1.27)) (justify left bottom))
@@
   (effects (font (size 1.27 1.27)) (justify left bottom))
 )
-(label "HUB_DS2_DM"
+(label "HUB_DS2_DN"
   (at 271.78 309.88 0)
   (effects (font (size 1.27 1.27)) (justify left bottom))
@@
   (effects (font (size 1.27 1.27)) (justify left bottom))
 )
-(label "HUB_DS3_DM"
+(label "HUB_DS3_DN"
   (at 546.1 269.24 0)
   (effects (font (size 1.27 1.27)) (justify left bottom))
 )
-(label "HUB_DS3_DM"
+(label "HUB_DS3_DN"
   (at 546.1 271.78 0)
   (effects (font (size 1.27 1.27)) (justify left bottom))
@@
   (effects (font (size 1.27 1.27)) (justify left bottom))
 )
-(label "HUB_DS3_DM"
+(label "HUB_DS3_DN"
   (at 556.26 309.88 0)
   (effects (font (size 1.27 1.27)) (justify left bottom))
